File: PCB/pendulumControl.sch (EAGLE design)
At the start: 27 parts, among them IC1 PIC32MX340F512H, IC2 LT1963EST-3.3

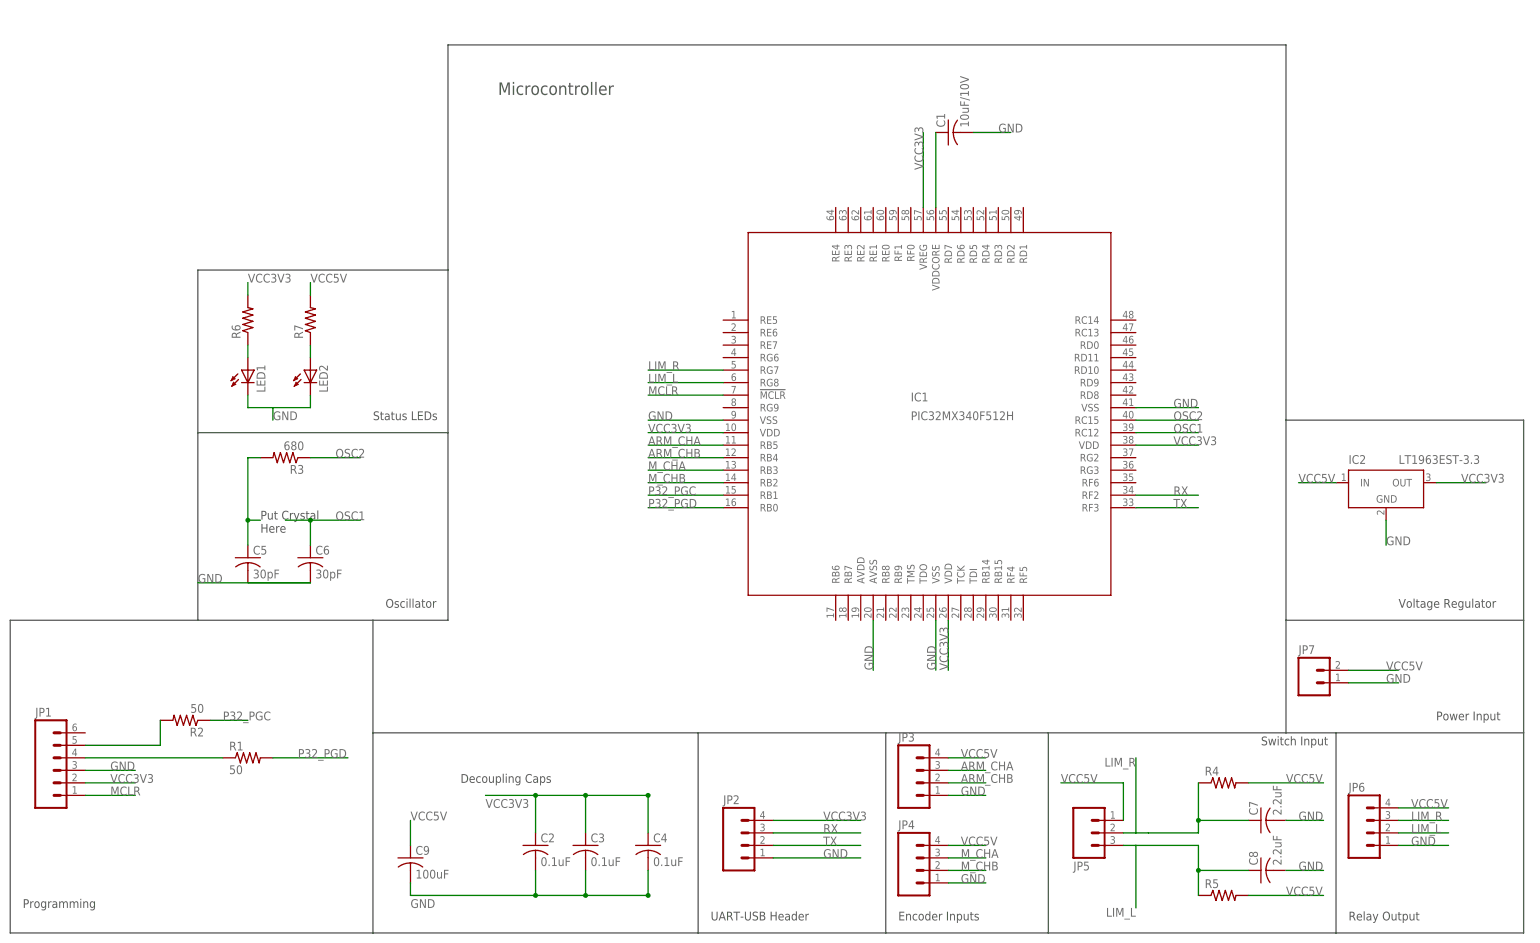
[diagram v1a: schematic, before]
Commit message: Added oscillator
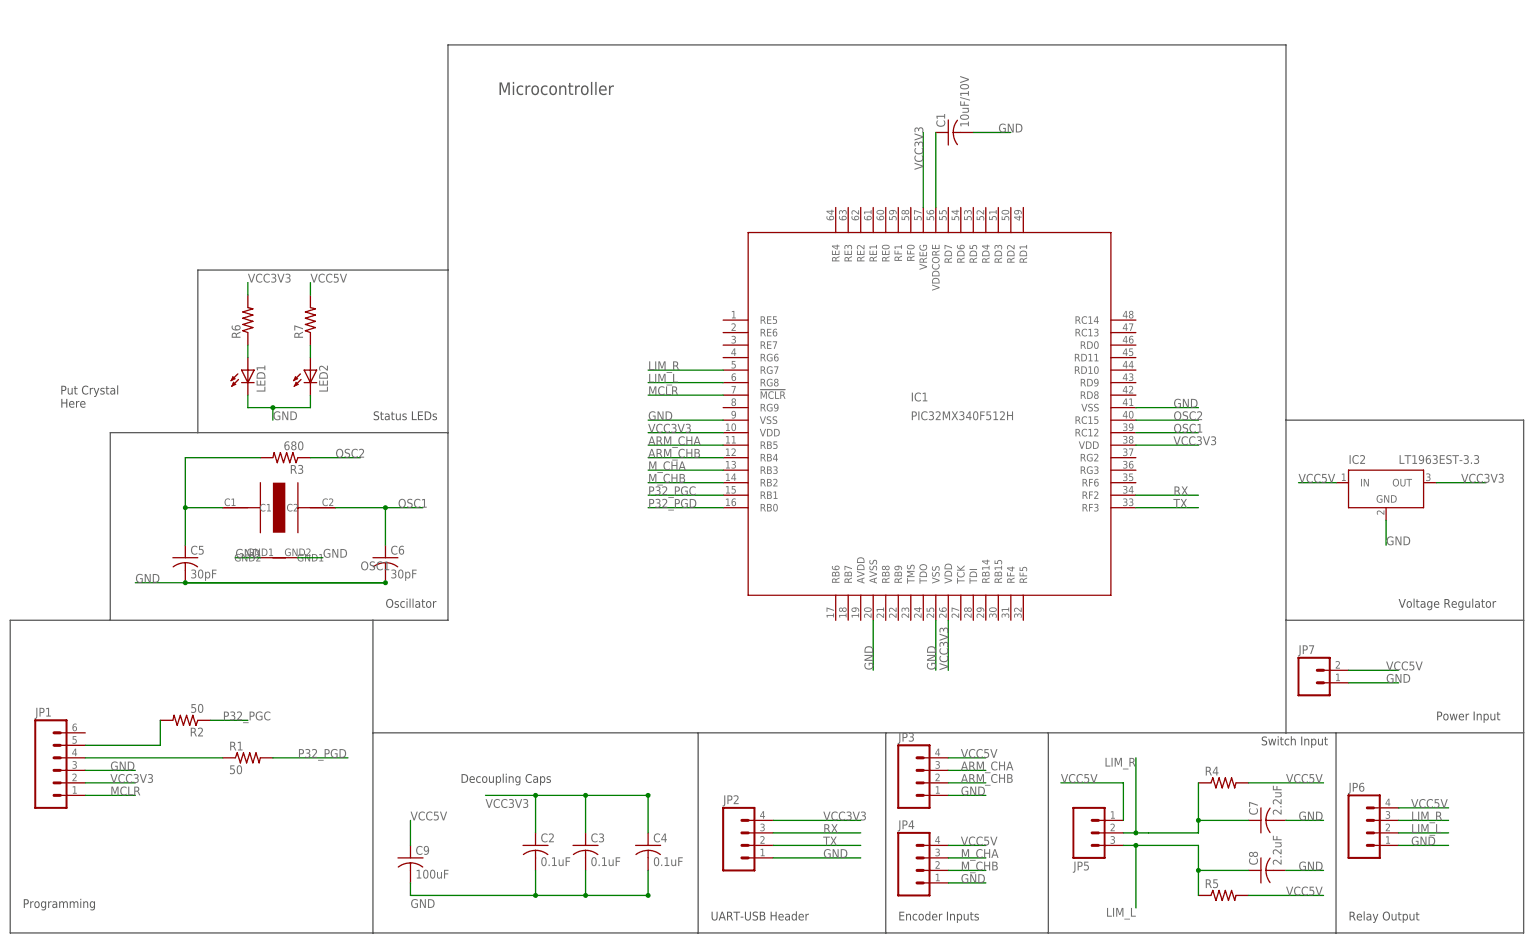
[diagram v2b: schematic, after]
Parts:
- added U$1: 7X5MMOSC, custom:7X5MMOSC
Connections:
- net GND: now also U$1.GND1, U$1.GND2
- net N$3: now also U$1.C1
- net OSC1: now also U$1.C2
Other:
- moved on the sheet: C5, C6
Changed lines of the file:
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@@
 <part name="JP7" library="SparkFun-Connectors" deviceset="M02" device="3.5MM"/>
 <part name="IC2" library="linear-technology" deviceset="LT1963EST" device="" technology="-3.3"/>
+<part name="U$1" library="custom" deviceset="7X5MMOSC" device=""/>
 </parts>
 <sheets>
@@
 <wire x1="99.06" y1="-68.58" x2="157.48" y2="-68.58" width="0.1524" layer="97"/>
 <wire x1="157.48" y1="-68.58" x2="195.58" y2="-68.58" width="0.1524" layer="97"/>
-<wire x1="-38.1" y1="-5.08" x2="-73.66" y2="-5.08" width="0.1524" layer="97"/>
-<wire x1="-73.66" y1="-5.08" x2="-111.76" y2="-5.08" width="0.1524" layer="97"/>
+<wire x1="-38.1" y1="-5.08" x2="-91.44" y2="-5.08" width="0.1524" layer="97"/>
+<wire x1="-91.44" y1="-5.08" x2="-111.76" y2="-5.08" width="0.1524" layer="97"/>
 <wire x1="-111.76" y1="-5.08" x2="-111.76" y2="-68.58" width="0.1524" layer="97"/>
 <text x="-109.22" y="-63.5" size="1.778" layer="97">Programming</text>
@@
 <wire x1="27.94" y1="-27.94" x2="27.94" y2="-68.58" width="0.1524" layer="97"/>
 <text x="-20.32" y="-38.1" size="1.778" layer="97">Decoupling Caps</text>
-<wire x1="-73.66" y1="-5.08" x2="-73.66" y2="33.02" width="0.1524" layer="97"/>
+<wire x1="-91.44" y1="-5.08" x2="-91.44" y2="33.02" width="0.1524" layer="97"/>
 <wire x1="-73.66" y1="33.02" x2="-22.86" y2="33.02" width="0.1524" layer="97"/>
 <text x="-35.56" y="-2.54" size="1.778" layer="97">Oscillator</text>
-<text x="-60.96" y="12.7" size="1.778" layer="97">Put Crystal
+<text x="-101.6" y="38.1" size="1.778" layer="97">Put Crystal
 Here</text>
 <wire x1="27.94" y1="-27.94" x2="66.04" y2="-27.94" width="0.1524" layer="97"/>
@@
 <wire x1="147.32" y1="35.56" x2="147.32" y2="-5.08" width="0.1524" layer="97"/>
 <wire x1="147.32" y1="-5.08" x2="147.32" y2="-27.94" width="0.1524" layer="97"/>
+<wire x1="-91.44" y1="33.02" x2="-73.66" y2="33.02" width="0.1524" layer="97"/>
 <wire x1="-73.66" y1="33.02" x2="-73.66" y2="66.04" width="0.1524" layer="97"/>
 <wire x1="-73.66" y1="66.04" x2="-22.86" y2="66.04" width="0.1524" layer="97"/>
@@
 <instance part="C3" gate="G$1" x="5.08" y="-50.8"/>
 <instance part="C4" gate="G$1" x="17.78" y="-50.8"/>
-<instance part="C5" gate="G$1" x="-63.5" y="7.62"/>
-<instance part="C6" gate="G$1" x="-50.8" y="7.62"/>
+<instance part="C5" gate="G$1" x="-76.2" y="7.62"/>
+<instance part="C6" gate="G$1" x="-35.56" y="7.62"/>
 <instance part="R3" gate="G$1" x="-55.88" y="27.94" rot="R180"/>
 <instance part="JP2" gate="G$1" x="38.1" y="-50.8"/>
@@
 <instance part="JP7" gate="G$1" x="152.4" y="-17.78"/>
 <instance part="IC2" gate="G$1" x="167.64" y="20.32"/>
+<instance part="U$1" gate="G$1" x="-55.88" y="17.78"/>
 </instances>
 <busses>
@@
 <pinref part="C5" gate="G$1" pin="2"/>
 <pinref part="C6" gate="G$1" pin="2"/>
-<wire x1="-63.5" y1="2.54" x2="-50.8" y2="2.54" width="0.1524" layer="91"/>
-<wire x1="-50.8" y1="2.54" x2="-73.66" y2="2.54" width="0.1524" layer="91"/>
-<label x="-73.66" y="2.54" size="1.778" layer="95"/>
+<wire x1="-76.2" y1="2.54" x2="-35.56" y2="2.54" width="0.1524" layer="91"/>
+<wire x1="-35.56" y1="2.54" x2="-76.2" y2="2.54" width="0.1524" layer="91"/>
+<label x="-86.36" y="2.54" size="1.778" layer="95"/>
+<junction x="-35.56" y="2.54"/>
+<junction x="-76.2" y="2.54"/>
+<wire x1="-76.2" y1="2.54" x2="-86.36" y2="2.54" width="0.1524" layer="91"/>
 </segment>
 <segment>
@@
 <wire x1="-58.42" y1="38.1" x2="-58.42" y2="35.56" width="0.1524" layer="91"/>
 <label x="-58.42" y="35.56" size="1.778" layer="97"/>
+<junction x="-58.42" y="38.1"/>
 </segment>
 <segment>
@@
 <wire x1="167.64" y1="15.24" x2="167.64" y2="10.16" width="0.1524" layer="91"/>
 <label x="167.64" y="10.16" size="1.778" layer="95"/>
+</segment>
+<segment>
+<pinref part="U$1" gate="G$1" pin="GND1"/>
+<wire x1="-60.96" y1="7.62" x2="-66.04" y2="7.62" width="0.1524" layer="91"/>
+<label x="-66.04" y="7.62" size="1.778" layer="95"/>
+</segment>
+<segment>
+<pinref part="U$1" gate="G$1" pin="GND2"/>
+<wire x1="-53.34" y1="7.62" x2="-48.26" y2="7.62" width="0.1524" layer="91"/>
+<label x="-48.26" y="7.62" size="1.778" layer="95"/>
 </segment>
 </net>
@@
 <pinref part="R3" gate="G$1" pin="2"/>
 <pinref part="C5" gate="G$1" pin="1"/>
-<wire x1="-60.96" y1="27.94" x2="-63.5" y2="27.94" width="0.1524" layer="91"/>
-<wire x1="-63.5" y1="27.94" x2="-63.5" y2="15.24" width="0.1524" layer="91"/>
-<wire x1="-63.5" y1="15.24" x2="-63.5" y2="10.16" width="0.1524" layer="91"/>
-<wire x1="-63.5" y1="15.24" x2="-60.96" y2="15.24" width="0.1524" layer="91"/>
-<junction x="-63.5" y="15.24"/>
+<wire x1="-60.96" y1="27.94" x2="-76.2" y2="27.94" width="0.1524" layer="91"/>
+<wire x1="-76.2" y1="27.94" x2="-76.2" y2="17.78" width="0.1524" layer="91"/>
+<wire x1="-76.2" y1="17.78" x2="-76.2" y2="10.16" width="0.1524" layer="91"/>
+<junction x="-76.2" y="17.78"/>
+<pinref part="U$1" gate="G$1" pin="C1"/>
+<wire x1="-76.2" y1="17.78" x2="-68.58" y2="17.78" width="0.1524" layer="91"/>
 </segment>
 </net>
@@
 <net name="OSC1" class="0">
 <segment>
+<wire x1="-45.72" y1="17.78" x2="-35.56" y2="17.78" width="0.1524" layer="91"/>
+<label x="-40.64" y="5.08" size="1.778" layer="95"/>
+<pinref part="U$1" gate="G$1" pin="C2"/>
+<label x="-33.02" y="17.78" size="1.778" layer="95"/>
 <pinref part="C6" gate="G$1" pin="1"/>
-<wire x1="-50.8" y1="10.16" x2="-50.8" y2="15.24" width="0.1524" layer="91"/>
-<wire x1="-50.8" y1="15.24" x2="-40.64" y2="15.24" width="0.1524" layer="91"/>
-<label x="-45.72" y="15.24" size="1.778" layer="95"/>
-<wire x1="-50.8" y1="15.24" x2="-55.88" y2="15.24" width="0.1524" layer="91"/>
-<junction x="-50.8" y="15.24"/>
+<wire x1="-35.56" y1="10.16" x2="-35.56" y2="17.78" width="0.1524" layer="91"/>
+<wire x1="-35.56" y1="17.78" x2="-27.94" y2="17.78" width="0.1524" layer="91"/>
+<junction x="-35.56" y="17.78"/>
 </segment>
 <segment>
@@
 <wire x1="116.84" y1="-48.26" x2="116.84" y2="-33.02" width="0.1524" layer="91"/>
 <label x="116.84" y="-33.02" size="1.778" layer="95" rot="R180"/>
+<junction x="116.84" y="-48.26"/>
 </segment>
 <segment>
@@
 <wire x1="116.84" y1="-50.8" x2="116.84" y2="-63.5" width="0.1524" layer="91"/>
 <label x="116.84" y="-63.5" size="1.778" layer="95" rot="R180"/>
-</segment>
-<segment>
+<junction x="116.84" y="-50.8"/>
+</segment>
+<segment>

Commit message: Completed first routing.
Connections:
- net VCC3V3: now also IC1.AVDD
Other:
- moved on the sheet: R3
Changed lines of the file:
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@@
 <instance part="C5" gate="G$1" x="-76.2" y="7.62"/>
 <instance part="C6" gate="G$1" x="-35.56" y="7.62"/>
-<instance part="R3" gate="G$1" x="-55.88" y="27.94" rot="R180"/>
+<instance part="R3" gate="G$1" x="-68.58" y="27.94" rot="R180"/>
 <instance part="JP2" gate="G$1" x="38.1" y="-50.8"/>
 <instance part="JP3" gate="G$1" x="73.66" y="-38.1"/>
@@
 <segment>
 <pinref part="U$1" gate="G$1" pin="GND1"/>
-<wire x1="-60.96" y1="7.62" x2="-66.04" y2="7.62" width="0.1524" layer="91"/>
-<label x="-66.04" y="7.62" size="1.778" layer="95"/>
+<wire x1="-55.82" y1="11.5" x2="-55.88" y2="7.62" width="0.1524" layer="91"/>
+<label x="-55.88" y="7.62" size="1.778" layer="95"/>
 </segment>
 <segment>
 <pinref part="U$1" gate="G$1" pin="GND2"/>
-<wire x1="-53.34" y1="7.62" x2="-48.26" y2="7.62" width="0.1524" layer="91"/>
-<label x="-48.26" y="7.62" size="1.778" layer="95"/>
+<wire x1="-55.82" y1="24.32" x2="-55.88" y2="25.4" width="0.1524" layer="91"/>
+<label x="-55.88" y="25.4" size="1.778" layer="95"/>
 </segment>
 </net>
@@
 <label x="182.88" y="22.86" size="1.778" layer="95"/>
 </segment>
+<segment>
+<pinref part="IC1" gate="G$1" pin="AVDD"/>
+<wire x1="60.96" y1="-5.08" x2="60.96" y2="-15.24" width="0.1524" layer="91"/>
+<label x="60.96" y="-15.24" size="1.778" layer="95" rot="R90"/>
+</segment>
 </net>
 <net name="N$10" class="0">
@@
 <pinref part="R3" gate="G$1" pin="2"/>
 <pinref part="C5" gate="G$1" pin="1"/>
-<wire x1="-60.96" y1="27.94" x2="-76.2" y2="27.94" width="0.1524" layer="91"/>
+<wire x1="-73.66" y1="27.94" x2="-76.2" y2="27.94" width="0.1524" layer="91"/>
 <wire x1="-76.2" y1="27.94" x2="-76.2" y2="17.78" width="0.1524" layer="91"/>
 <wire x1="-76.2" y1="17.78" x2="-76.2" y2="10.16" width="0.1524" layer="91"/>
 <junction x="-76.2" y="17.78"/>
 <pinref part="U$1" gate="G$1" pin="C1"/>
-<wire x1="-76.2" y1="17.78" x2="-68.58" y2="17.78" width="0.1524" layer="91"/>
+<wire x1="-76.2" y1="17.78" x2="-63.08" y2="17.78" width="0.1524" layer="91"/>
 </segment>
 </net>
@@
 <segment>
 <pinref part="R3" gate="G$1" pin="1"/>
-<wire x1="-50.8" y1="27.94" x2="-40.64" y2="27.94" width="0.1524" layer="91"/>
-<label x="-45.72" y="27.94" size="1.778" layer="95"/>
+<wire x1="-63.5" y1="27.94" x2="-58.42" y2="27.94" width="0.1524" layer="91"/>
+<label x="-63.5" y="27.94" size="1.778" layer="95"/>
 </segment>
 <segment>
@@
 <net name="OSC1" class="0">
 <segment>
-<wire x1="-45.72" y1="17.78" x2="-35.56" y2="17.78" width="0.1524" layer="91"/>
+<wire x1="-48.42" y1="17.78" x2="-35.56" y2="17.78" width="0.1524" layer="91"/>
 <label x="-40.64" y="5.08" size="1.778" layer="95"/>
 <pinref part="U$1" gate="G$1" pin="C2"/>

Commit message: Fixed Header on wrong side of board
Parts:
- JP2: device SparkFun-Connectors:M04LOCK_LONGPADS -> SparkFun-Connectors:M04PTH
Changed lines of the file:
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@@
 <part name="C6" library="rcl" deviceset="C-US" device="C0805" value="30pF"/>
 <part name="R3" library="rcl" deviceset="R-US_" device="R0805" value="680"/>
-<part name="JP2" library="SparkFun-Connectors" deviceset="M04" device="LOCK_LONGPADS"/>
+<part name="JP2" library="SparkFun-Connectors" deviceset="M04" device="PTH"/>
 <part name="JP3" library="SparkFun-Connectors" deviceset="M04" device="PTH"/>
 <part name="JP4" library="SparkFun-Connectors" deviceset="M04" device="PTH"/>

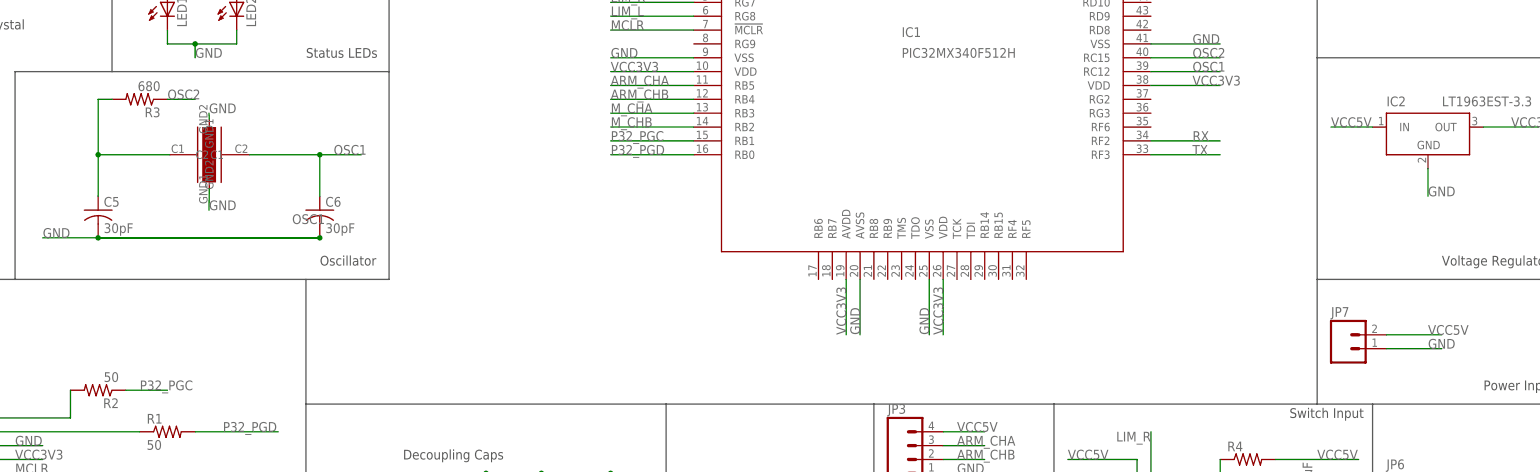
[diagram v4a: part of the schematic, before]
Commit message: Changed Crystal and power input. Crystal now has clear zone.
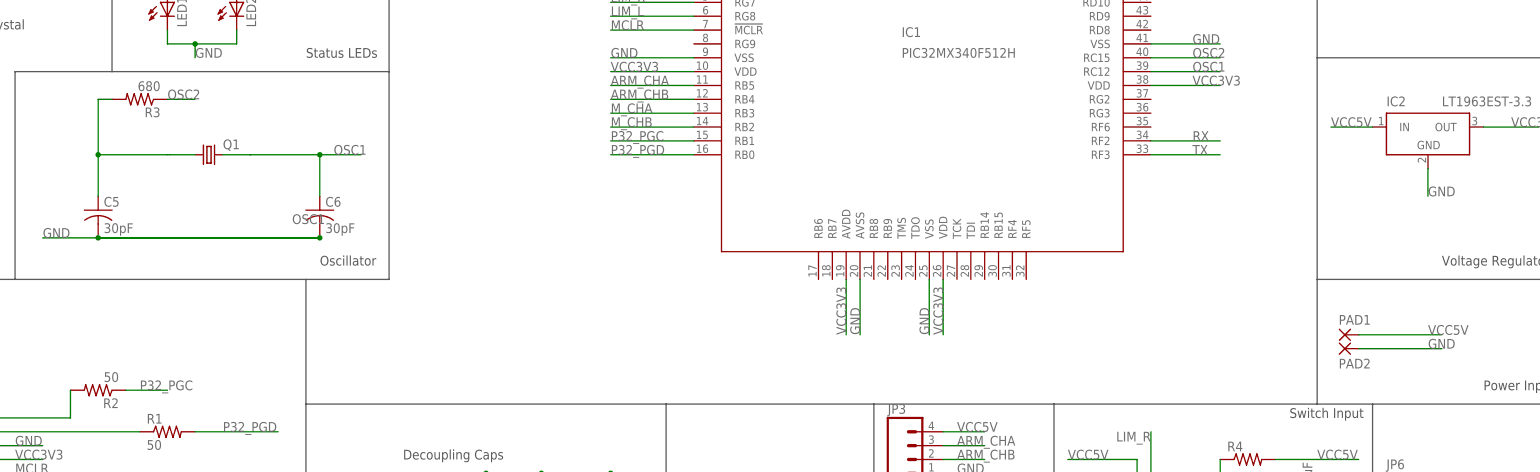
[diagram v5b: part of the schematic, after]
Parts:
- removed JP7: (no value), SparkFun-Connectors:M023.5MM
- removed U$1: 7X5MMOSC, custom:7X5MMOSC
- added PAD1, PAD2: (no value), wirepad:3,81/1,4
- added Q1: (no value), crystal:CRYSTALHC49S
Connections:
- net GND: now also PAD2.P; no longer JP7.1, U$1.GND1, U$1.GND2
- net N$3: now also Q1.1; no longer U$1.C1
- net OSC1: now also Q1.2; no longer U$1.C2
- net VCC5V: now also PAD1.P; no longer JP7.2
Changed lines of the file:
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@@
 <part name="R6" library="rcl" deviceset="R-US_" device="R0805"/>
 <part name="R7" library="rcl" deviceset="R-US_" device="R0805"/>
-<part name="JP7" library="SparkFun-Connectors" deviceset="M02" device="3.5MM"/>
 <part name="IC2" library="linear-technology" deviceset="LT1963EST" device="" technology="-3.3"/>
-<part name="U$1" library="custom" deviceset="7X5MMOSC" device=""/>
+<part name="Q1" library="crystal" deviceset="CRYSTAL" device="HC49S"/>
+<part name="PAD1" library="wirepad" deviceset="3,81/1,4" device=""/>
+<part name="PAD2" library="wirepad" deviceset="3,81/1,4" device=""/>
 </parts>
 <sheets>
@@
 <instance part="R6" gate="G$1" x="-63.5" y="55.88" rot="R90"/>
 <instance part="R7" gate="G$1" x="-50.8" y="55.88" rot="R90"/>
-<instance part="JP7" gate="G$1" x="152.4" y="-17.78"/>
 <instance part="IC2" gate="G$1" x="167.64" y="20.32"/>
-<instance part="U$1" gate="G$1" x="-55.88" y="17.78"/>
+<instance part="Q1" gate="G$1" x="-55.88" y="17.78"/>
+<instance part="PAD1" gate="1" x="152.4" y="-15.24"/>
+<instance part="PAD2" gate="1" x="152.4" y="-17.78" rot="MR180"/>
 </instances>
 <busses>
@@
 </segment>
 <segment>
-<pinref part="JP7" gate="G$1" pin="1"/>
-<wire x1="160.02" y1="-17.78" x2="170.18" y2="-17.78" width="0.1524" layer="91"/>
+<wire x1="154.94" y1="-17.78" x2="170.18" y2="-17.78" width="0.1524" layer="91"/>
 <label x="167.64" y="-17.78" size="1.778" layer="95"/>
+<pinref part="PAD2" gate="1" pin="P"/>
 </segment>
 <segment>
@@
 <wire x1="167.64" y1="15.24" x2="167.64" y2="10.16" width="0.1524" layer="91"/>
 <label x="167.64" y="10.16" size="1.778" layer="95"/>
-</segment>
-<segment>
-<pinref part="U$1" gate="G$1" pin="GND1"/>
-<wire x1="-55.82" y1="11.5" x2="-55.88" y2="7.62" width="0.1524" layer="91"/>
-<label x="-55.88" y="7.62" size="1.778" layer="95"/>
-</segment>
-<segment>
-<pinref part="U$1" gate="G$1" pin="GND2"/>
-<wire x1="-55.82" y1="24.32" x2="-55.88" y2="25.4" width="0.1524" layer="91"/>
-<label x="-55.88" y="25.4" size="1.778" layer="95"/>
 </segment>
 </net>
@@
 <wire x1="-76.2" y1="17.78" x2="-76.2" y2="10.16" width="0.1524" layer="91"/>
 <junction x="-76.2" y="17.78"/>
-<pinref part="U$1" gate="G$1" pin="C1"/>
-<wire x1="-76.2" y1="17.78" x2="-63.08" y2="17.78" width="0.1524" layer="91"/>
+<wire x1="-76.2" y1="17.78" x2="-63.5" y2="17.78" width="0.1524" layer="91"/>
+<pinref part="Q1" gate="G$1" pin="1"/>
+<wire x1="-63.5" y1="17.78" x2="-63.08" y2="17.78" width="0.1524" layer="91"/>
+<wire x1="-63.08" y1="17.78" x2="-58.42" y2="17.78" width="0.1524" layer="91"/>
 </segment>
 </net>
@@
 <net name="OSC1" class="0">
 <segment>
-<wire x1="-48.42" y1="17.78" x2="-35.56" y2="17.78" width="0.1524" layer="91"/>
+<wire x1="-48.42" y1="17.78" x2="-48.26" y2="17.78" width="0.1524" layer="91"/>
 <label x="-40.64" y="5.08" size="1.778" layer="95"/>
-<pinref part="U$1" gate="G$1" pin="C2"/>
 <label x="-33.02" y="17.78" size="1.778" layer="95"/>
 <pinref part="C6" gate="G$1" pin="1"/>
+<wire x1="-48.26" y1="17.78" x2="-35.56" y2="17.78" width="0.1524" layer="91"/>
 <wire x1="-35.56" y1="10.16" x2="-35.56" y2="17.78" width="0.1524" layer="91"/>
 <wire x1="-35.56" y1="17.78" x2="-27.94" y2="17.78" width="0.1524" layer="91"/>
 <junction x="-35.56" y="17.78"/>
+<pinref part="Q1" gate="G$1" pin="2"/>
+<wire x1="-53.34" y1="17.78" x2="-48.42" y2="17.78" width="0.1524" layer="91"/>
 </segment>
 <segment>
@@
 </segment>
 <segment>
-<pinref part="JP7" gate="G$1" pin="2"/>
-<wire x1="160.02" y1="-15.24" x2="170.18" y2="-15.24" width="0.1524" layer="91"/>
+<wire x1="154.94" y1="-15.24" x2="170.18" y2="-15.24" width="0.1524" layer="91"/>
 <label x="167.64" y="-15.24" size="1.778" layer="95"/>
-</segment>
-<segment>
+<pinref part="PAD1" gate="1" pin="P"/>
+</segment>
+<segment>
